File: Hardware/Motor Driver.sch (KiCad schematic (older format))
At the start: 18 parts, among them U4 DRV8874

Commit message: schematic fixed
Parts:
- removed C10: 1uF, Resistor_SMD:R_0603_1608Metric, symbol Device:C_Small
- removed C13: 10uF, Capacitor_SMD:C_2220_5650Metric, symbol Device:C_Small
- removed C17: 100nF, Resistor_SMD:R_0603_1608Metric, symbol Device:C_Small
- removed C20: 22nF, Resistor_SMD:R_0603_1608Metric, symbol Device:C_Small
- removed R13: 5.5k, Resistor_SMD:R_0603_1608Metric, symbol Device:R_Small_US
- removed R14: 16k, Resistor_SMD:R_0603_1608Metric, symbol Device:R_Small_US
- removed R17: 50k, Resistor_SMD:R_0603_1608Metric, symbol Device:R_Small_US
- removed R9: 10k, Resistor_SMD:R_0603_1608Metric, symbol Device:R_Small_US
- removed U4: DRV8874, Package_SO:HTSSOP-16-1EP_4.4x5mm_P0.65mm_EP3.4x5mm_Mask3x3mm_ThermalVias, symbol Driver_Motor:DRV8874
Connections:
- wire segments 50 -> 25
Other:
- moved on the sheet: C10, C13, C17, C20, R13, R14, R17, R9

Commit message: Readme updated
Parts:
- renumbered C10 to C14, C13 to C15, C17 to C16, C20 to C17, R9 to R11, R13 to R12, R14 to R13, R17 to R14, U4 to U5
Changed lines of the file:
@@
 P 5850 4500
 AR Path="/5FF172EF" Ref="#PWR?"  Part="1"
-AR Path="/5FF00151/5FF172EF" Ref="#PWR039"  Part="1"
-AR Path="/5FF2CF13/5FF172EF" Ref="#PWR039"  Part="1"
-F 0 "#PWR039" H 5850 4250 50  0001 C CNN
+AR Path="/5FF00151/5FF172EF" Ref="#PWR027"  Part="1"
+AR Path="/5FF2CF13/5FF172EF" Ref="#PWR036"  Part="1"
+F 0 "#PWR036" H 5850 4250 50  0001 C CNN
 F 1 "GND" H 5855 4327 50  0000 C CNN
 F 2 "" H 5850 4500 50  0001 C CNN
@@
 AR Path="/5EA2026E/5FF2BF81" Ref="C?"  Part="1"
 AR Path="/5FF2BF81" Ref="C?"  Part="1"
-AR Path="/5FF00151/5FF2BF81" Ref="C20"  Part="1"
-AR Path="/5FF2CF13/5FF2BF81" Ref="C20"  Part="1"
-F 0 "C20" H 6542 3396 50  0000 L CNN
+AR Path="/5FF00151/5FF2BF81" Ref="C17"  Part="1"
+AR Path="/5FF2CF13/5FF2BF81" Ref="C21"  Part="1"
+F 0 "C21" H 6542 3396 50  0000 L CNN
 F 1 "22nF" H 6542 3305 50  0000 L CNN
 F 2 "Resistor_SMD:R_0603_1608Metric" H 6450 3350 50  0001 C CNN
@@
 P 4850 4400
 AR Path="/5FF2D4A0" Ref="#PWR?"  Part="1"
-AR Path="/5FF00151/5FF2D4A0" Ref="#PWR038"  Part="1"
-AR Path="/5FF2CF13/5FF2D4A0" Ref="#PWR038"  Part="1"
-F 0 "#PWR038" H 4850 4250 50  0001 C CNN
+AR Path="/5FF00151/5FF2D4A0" Ref="#PWR026"  Part="1"
+AR Path="/5FF2CF13/5FF2D4A0" Ref="#PWR035"  Part="1"
+F 0 "#PWR035" H 4850 4250 50  0001 C CNN
 F 1 "+3.3V" H 4865 4573 50  0000 C CNN
 F 2 "" H 4850 4400 50  0001 C CNN
@@
 P 5000 4450
 AR Path="/5FF172DB" Ref="R?"  Part="1"
-AR Path="/5FF00151/5FF172DB" Ref="R14"  Part="1"
-AR Path="/5FF2CF13/5FF172DB" Ref="R14"  Part="1"
-F 0 "R14" V 5100 4450 50  0000 C CNN
+AR Path="/5FF00151/5FF172DB" Ref="R13"  Part="1"
+AR Path="/5FF2CF13/5FF172DB" Ref="R17"  Part="1"
+F 0 "R17" V 5100 4450 50  0000 C CNN
 F 1 "16k" V 4900 4450 50  0000 C CNN
 F 2 "Resistor_SMD:R_0603_1608Metric" H 5000 4450 50  0001 C CNN
@@
 P 7400 2750
 AR Path="/5FF2D498" Ref="#PWR?"  Part="1"
-AR Path="/5FF00151/5FF2D498" Ref="#PWR018"  Part="1"
-AR Path="/5FF2CF13/5FF2D498" Ref="#PWR018"  Part="1"
-F 0 "#PWR018" H 7200 2600 50  0001 C CNN
+AR Path="/5FF00151/5FF2D498" Ref="#PWR020"  Part="1"
+AR Path="/5FF2CF13/5FF2D498" Ref="#PWR029"  Part="1"
+F 0 "#PWR029" H 7200 2600 50  0001 C CNN
 F 1 "Vdrive" H 7415 2923 50  0000 C CNN
 F 2 "" H 7400 2750 50  0001 C CNN
@@
 P 7100 2750
 AR Path="/5FF172EC" Ref="#PWR?"  Part="1"
-AR Path="/5FF00151/5FF172EC" Ref="#PWR016"  Part="1"
-AR Path="/5FF2CF13/5FF172EC" Ref="#PWR016"  Part="1"
-F 0 "#PWR016" H 6900 2600 50  0001 C CNN
+AR Path="/5FF00151/5FF172EC" Ref="#PWR019"  Part="1"
+AR Path="/5FF2CF13/5FF172EC" Ref="#PWR028"  Part="1"
+F 0 "#PWR028" H 6900 2600 50  0001 C CNN
 F 1 "Vdrive" H 7115 2923 50  0000 C CNN
 F 2 "" H 7100 2750 50  0001 C CNN
@@
 P 7100 2850
 AR Path="/5FF172D6" Ref="C?"  Part="1"
-AR Path="/5FF00151/5FF172D6" Ref="C10"  Part="1"
-AR Path="/5FF2CF13/5FF172D6" Ref="C10"  Part="1"
-F 0 "C10" H 7192 2896 50  0000 L CNN
+AR Path="/5FF00151/5FF172D6" Ref="C14"  Part="1"
+AR Path="/5FF2CF13/5FF172D6" Ref="C18"  Part="1"
+F 0 "C18" H 7192 2896 50  0000 L CNN
 F 1 "1uF" H 7192 2805 50  0000 L CNN
 F 2 "Resistor_SMD:R_0603_1608Metric" H 7100 2850 50  0001 C CNN
@@
 P 7100 2950
 AR Path="/5FF2BF19" Ref="#PWR?"  Part="1"
-AR Path="/5FF00151/5FF2BF19" Ref="#PWR026"  Part="1"
-AR Path="/5FF2CF13/5FF2BF19" Ref="#PWR026"  Part="1"
-F 0 "#PWR026" H 7100 2700 50  0001 C CNN
+AR Path="/5FF00151/5FF2BF19" Ref="#PWR022"  Part="1"
+AR Path="/5FF2CF13/5FF2BF19" Ref="#PWR031"  Part="1"
+F 0 "#PWR031" H 7100 2700 50  0001 C CNN
 F 1 "GND" H 7105 2777 50  0000 C CNN
 F 2 "" H 7100 2950 50  0001 C CNN
@@
 P 7400 2950
 AR Path="/5FF2D48C" Ref="#PWR?"  Part="1"
-AR Path="/5FF00151/5FF2D48C" Ref="#PWR027"  Part="1"
-AR Path="/5FF2CF13/5FF2D48C" Ref="#PWR027"  Part="1"
-F 0 "#PWR027" H 7400 2700 50  0001 C CNN
+AR Path="/5FF00151/5FF2D48C" Ref="#PWR023"  Part="1"
+AR Path="/5FF2CF13/5FF2D48C" Ref="#PWR032"  Part="1"
+F 0 "#PWR032" H 7400 2700 50  0001 C CNN
 F 1 "GND" H 7405 2777 50  0000 C CNN
 F 2 "" H 7400 2950 50  0001 C CNN
@@
 P 5000 4050
 AR Path="/5FF2D49F" Ref="#PWR?"  Part="1"
-AR Path="/5FF00151/5FF2D49F" Ref="#PWR035"  Part="1"
-AR Path="/5FF2CF13/5FF2D49F" Ref="#PWR035"  Part="1"
-F 0 "#PWR035" H 5000 3800 50  0001 C CNN
+AR Path="/5FF00151/5FF2D49F" Ref="#PWR025"  Part="1"
+AR Path="/5FF2CF13/5FF2D49F" Ref="#PWR034"  Part="1"
+F 0 "#PWR034" H 5000 3800 50  0001 C CNN
 F 1 "GND" V 5005 3922 50  0000 R CNN
 F 2 "" H 5000 4050 50  0001 C CNN
@@
 AR Path="/5EA2026E/5FF2D494" Ref="R?"  Part="1"
 AR Path="/5FF2D494" Ref="R?"  Part="1"
-AR Path="/5FF00151/5FF2D494" Ref="R9"  Part="1"
-AR Path="/5FF2CF13/5FF2D494" Ref="R9"  Part="1"
-F 0 "R9" H 4968 3646 50  0000 L CNN
+AR Path="/5FF00151/5FF2D494" Ref="R11"  Part="1"
+AR Path="/5FF2CF13/5FF2D494" Ref="R15"  Part="1"
+F 0 "R15" H 4968 3646 50  0000 L CNN
 F 1 "10k" H 4968 3555 50  0000 L CNN
 F 2 "Resistor_SMD:R_0603_1608Metric" H 4900 3600 50  0001 C CNN
@@
 P 7400 2850
 AR Path="/5FF2D490" Ref="C?"  Part="1"
-AR Path="/5FF00151/5FF2D490" Ref="C13"  Part="1"
-AR Path="/5FF2CF13/5FF2D490" Ref="C13"  Part="1"
-F 0 "C13" H 7492 2896 50  0000 L CNN
+AR Path="/5FF00151/5FF2D490" Ref="C15"  Part="1"
+AR Path="/5FF2CF13/5FF2D490" Ref="C19"  Part="1"
+F 0 "C19" H 7492 2896 50  0000 L CNN
 F 1 "10uF" H 7492 2805 50  0000 L CNN
 F 2 "Capacitor_SMD:C_2220_5650Metric" H 7400 2850 50  0001 C CNN
@@
 P 5850 3050
 AR Path="/5FF172F1" Ref="U?"  Part="1"
-AR Path="/5FF00151/5FF172F1" Ref="U4"  Part="1"
-AR Path="/5FF2CF13/5FF172F1" Ref="U4"  Part="1"
-F 0 "U4" H 6250 3250 50  0000 C CNN
+AR Path="/5FF00151/5FF172F1" Ref="U5"  Part="1"
+AR Path="/5FF2CF13/5FF172F1" Ref="U6"  Part="1"
+F 0 "U6" H 6250 3250 50  0000 C CNN
 F 1 "DRV8874" H 6250 3150 50  0000 C CNN
 F 2 "Package_SO:HTSSOP-16-1EP_4.4x5mm_P0.65mm_EP3.4x5mm_Mask3x3mm_ThermalVias" H 6200 3200 50  0001 C CNN
@@
 P 4900 3500
 AR Path="/5FF172E1" Ref="#PWR?"  Part="1"
-AR Path="/5FF00151/5FF172E1" Ref="#PWR030"  Part="1"
-AR Path="/5FF2CF13/5FF172E1" Ref="#PWR030"  Part="1"
-F 0 "#PWR030" H 4900 3350 50  0001 C CNN
+AR Path="/5FF00151/5FF172E1" Ref="#PWR024"  Part="1"
+AR Path="/5FF2CF13/5FF172E1" Ref="#PWR033"  Part="1"
+F 0 "#PWR033" H 4900 3350 50  0001 C CNN
 F 1 "+3.3V" H 4915 3673 50  0000 C CNN
 F 2 "" H 4900 3500 50  0001 C CNN
@@
 P 5100 4050
 AR Path="/5FF2D49E" Ref="R?"  Part="1"
-AR Path="/5FF00151/5FF2D49E" Ref="R13"  Part="1"
-AR Path="/5FF2CF13/5FF2D49E" Ref="R13"  Part="1"
-F 0 "R13" V 5050 3950 50  0000 C CNN
+AR Path="/5FF00151/5FF2D49E" Ref="R12"  Part="1"
+AR Path="/5FF2CF13/5FF2D49E" Ref="R16"  Part="1"
+F 0 "R16" V 5050 3950 50  0000 C CNN
 F 1 "5.5k" V 5050 4150 50  0000 C CNN
 F 2 "Resistor_SMD:R_0603_1608Metric" H 5100 4050 50  0001 C CNN
@@
 P 5300 4450
 AR Path="/5FF172DD" Ref="R?"  Part="1"
-AR Path="/5FF00151/5FF172DD" Ref="R17"  Part="1"
-AR Path="/5FF2CF13/5FF172DD" Ref="R17"  Part="1"
-F 0 "R17" V 5400 4450 50  0000 C CNN
+AR Path="/5FF00151/5FF172DD" Ref="R14"  Part="1"
+AR Path="/5FF2CF13/5FF172DD" Ref="R18"  Part="1"
+F 0 "R18" V 5400 4450 50  0000 C CNN
 F 1 "50k" V 5200 4450 50  0000 C CNN
 F 2 "Resistor_SMD:R_0603_1608Metric" H 5300 4450 50  0001 C CNN
@@
 P 6000 2850
 AR Path="/5FF2D4A1" Ref="#PWR?"  Part="1"
-AR Path="/5FF00151/5FF2D4A1" Ref="#PWR023"  Part="1"
-AR Path="/5FF2CF13/5FF2D4A1" Ref="#PWR023"  Part="1"
-F 0 "#PWR023" H 5800 2700 50  0001 C CNN
+AR Path="/5FF00151/5FF2D4A1" Ref="#PWR021"  Part="1"
+AR Path="/5FF2CF13/5FF2D4A1" Ref="#PWR030"  Part="1"
+F 0 "#PWR030" H 5800 2700 50  0001 C CNN
 F 1 "Vdrive" H 6015 3023 50  0000 C CNN
 F 2 "" H 6000 2850 50  0001 C CNN
@@
 P 5850 2900
 AR Path="/5FF2D4A2" Ref="C?"  Part="1"
-AR Path="/5FF00151/5FF2D4A2" Ref="C17"  Part="1"
-AR Path="/5FF2CF13/5FF2D4A2" Ref="C17"  Part="1"
-F 0 "C17" V 5650 2800 50  0000 C CNN
+AR Path="/5FF00151/5FF2D4A2" Ref="C16"  Part="1"
+AR Path="/5FF2CF13/5FF2D4A2" Ref="C20"  Part="1"
+F 0 "C20" V 5650 2800 50  0000 C CNN
 F 1 "100nF" V 5750 2800 50  0000 C CNN
 F 2 "Resistor_SMD:R_0603_1608Metric" H 5850 2900 50  0001 C CNN

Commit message: Signed-off-by: Usman Mehmood <usmanmehmood55@gmail.com>
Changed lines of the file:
@@
 $Descr A4 11693 8268
 encoding utf-8
-Sheet 6 6
+Sheet 2 9
 Title ""
 Date ""
@@
 AR Path="/5FF00151/5FF172EF" Ref="#PWR027"  Part="1"
 AR Path="/5FF2CF13/5FF172EF" Ref="#PWR036"  Part="1"
-F 0 "#PWR036" H 5850 4250 50  0001 C CNN
+F 0 "#PWR027" H 5850 4250 50  0001 C CNN
 F 1 "GND" H 5855 4327 50  0000 C CNN
 F 2 "" H 5850 4500 50  0001 C CNN
@@
 AR Path="/5FF00151/5FF2BF81" Ref="C17"  Part="1"
 AR Path="/5FF2CF13/5FF2BF81" Ref="C21"  Part="1"
-F 0 "C21" H 6542 3396 50  0000 L CNN
+F 0 "C17" H 6542 3396 50  0000 L CNN
 F 1 "22nF" H 6542 3305 50  0000 L CNN
 F 2 "Resistor_SMD:R_0603_1608Metric" H 6450 3350 50  0001 C CNN
@@
 AR Path="/5FF00151/5FF2D4A0" Ref="#PWR026"  Part="1"
 AR Path="/5FF2CF13/5FF2D4A0" Ref="#PWR035"  Part="1"
-F 0 "#PWR035" H 4850 4250 50  0001 C CNN
+F 0 "#PWR026" H 4850 4250 50  0001 C CNN
 F 1 "+3.3V" H 4865 4573 50  0000 C CNN
 F 2 "" H 4850 4400 50  0001 C CNN
@@
 AR Path="/5FF00151/5FF172DB" Ref="R13"  Part="1"
 AR Path="/5FF2CF13/5FF172DB" Ref="R17"  Part="1"
-F 0 "R17" V 5100 4450 50  0000 C CNN
+F 0 "R13" V 5100 4450 50  0000 C CNN
 F 1 "16k" V 4900 4450 50  0000 C CNN
 F 2 "Resistor_SMD:R_0603_1608Metric" H 5000 4450 50  0001 C CNN
@@
 AR Path="/5FF00151/5FF2D498" Ref="#PWR020"  Part="1"
 AR Path="/5FF2CF13/5FF2D498" Ref="#PWR029"  Part="1"
-F 0 "#PWR029" H 7200 2600 50  0001 C CNN
+F 0 "#PWR020" H 7200 2600 50  0001 C CNN
 F 1 "Vdrive" H 7415 2923 50  0000 C CNN
 F 2 "" H 7400 2750 50  0001 C CNN
@@
 AR Path="/5FF00151/5FF172EC" Ref="#PWR019"  Part="1"
 AR Path="/5FF2CF13/5FF172EC" Ref="#PWR028"  Part="1"
-F 0 "#PWR028" H 6900 2600 50  0001 C CNN
+F 0 "#PWR019" H 6900 2600 50  0001 C CNN
 F 1 "Vdrive" H 7115 2923 50  0000 C CNN
 F 2 "" H 7100 2750 50  0001 C CNN
@@
 AR Path="/5FF00151/5FF172D6" Ref="C14"  Part="1"
 AR Path="/5FF2CF13/5FF172D6" Ref="C18"  Part="1"
-F 0 "C18" H 7192 2896 50  0000 L CNN
+F 0 "C14" H 7192 2896 50  0000 L CNN
 F 1 "1uF" H 7192 2805 50  0000 L CNN
 F 2 "Resistor_SMD:R_0603_1608Metric" H 7100 2850 50  0001 C CNN
@@
 AR Path="/5FF00151/5FF2BF19" Ref="#PWR022"  Part="1"
 AR Path="/5FF2CF13/5FF2BF19" Ref="#PWR031"  Part="1"
-F 0 "#PWR031" H 7100 2700 50  0001 C CNN
+F 0 "#PWR022" H 7100 2700 50  0001 C CNN
 F 1 "GND" H 7105 2777 50  0000 C CNN
 F 2 "" H 7100 2950 50  0001 C CNN
@@
 AR Path="/5FF00151/5FF2D48C" Ref="#PWR023"  Part="1"
 AR Path="/5FF2CF13/5FF2D48C" Ref="#PWR032"  Part="1"
-F 0 "#PWR032" H 7400 2700 50  0001 C CNN
+F 0 "#PWR023" H 7400 2700 50  0001 C CNN
 F 1 "GND" H 7405 2777 50  0000 C CNN
 F 2 "" H 7400 2950 50  0001 C CNN
@@
 AR Path="/5FF00151/5FF2D49F" Ref="#PWR025"  Part="1"
 AR Path="/5FF2CF13/5FF2D49F" Ref="#PWR034"  Part="1"
-F 0 "#PWR034" H 5000 3800 50  0001 C CNN
+F 0 "#PWR025" H 5000 3800 50  0001 C CNN
 F 1 "GND" V 5005 3922 50  0000 R CNN
 F 2 "" H 5000 4050 50  0001 C CNN
@@
 AR Path="/5FF00151/5FF2D494" Ref="R11"  Part="1"
 AR Path="/5FF2CF13/5FF2D494" Ref="R15"  Part="1"
-F 0 "R15" H 4968 3646 50  0000 L CNN
+F 0 "R11" H 4968 3646 50  0000 L CNN
 F 1 "10k" H 4968 3555 50  0000 L CNN
 F 2 "Resistor_SMD:R_0603_1608Metric" H 4900 3600 50  0001 C CNN
@@
 AR Path="/5FF00151/5FF2D490" Ref="C15"  Part="1"
 AR Path="/5FF2CF13/5FF2D490" Ref="C19"  Part="1"
-F 0 "C19" H 7492 2896 50  0000 L CNN
+F 0 "C15" H 7492 2896 50  0000 L CNN
 F 1 "10uF" H 7492 2805 50  0000 L CNN
 F 2 "Capacitor_SMD:C_2220_5650Metric" H 7400 2850 50  0001 C CNN
@@
 	1    0    0    -1
 $EndComp
-$Comp
-L Driver_Motor:DRV8874 U?
-U 1 1 5FF172F1
-P 5850 3050
-AR Path="/5FF172F1" Ref="U?"  Part="1"
-AR Path="/5FF00151/5FF172F1" Ref="U5"  Part="1"
-AR Path="/5FF2CF13/5FF172F1" Ref="U6"  Part="1"
-F 0 "U6" H 6250 3250 50  0000 C CNN
-F 1 "DRV8874" H 6250 3150 50  0000 C CNN
-F 2 "Package_SO:HTSSOP-16-1EP_4.4x5mm_P0.65mm_EP3.4x5mm_Mask3x3mm_ThermalVias" H 6200 3200 50  0001 C CNN
-F 3 "" H 6200 3200 50  0001 C CNN
-	1    5850 3050
-	1    0    0    -1
-$EndComp
 Text HLabel 5200 3900 0    50   Output ~ 0
 iPROPI
@@
 AR Path="/5FF00151/5FF172E1" Ref="#PWR024"  Part="1"
 AR Path="/5FF2CF13/5FF172E1" Ref="#PWR033"  Part="1"
-F 0 "#PWR033" H 4900 3350 50  0001 C CNN
+F 0 "#PWR024" H 4900 3350 50  0001 C CNN
 F 1 "+3.3V" H 4915 3673 50  0000 C CNN
 F 2 "" H 4900 3500 50  0001 C CNN
@@
 AR Path="/5FF00151/5FF2D49E" Ref="R12"  Part="1"
 AR Path="/5FF2CF13/5FF2D49E" Ref="R16"  Part="1"
-F 0 "R16" V 5050 3950 50  0000 C CNN
+F 0 "R12" V 5050 3950 50  0000 C CNN
 F 1 "5.5k" V 5050 4150 50  0000 C CNN
 F 2 "Resistor_SMD:R_0603_1608Metric" H 5100 4050 50  0001 C CNN
@@
 AR Path="/5FF00151/5FF172DD" Ref="R14"  Part="1"
 AR Path="/5FF2CF13/5FF172DD" Ref="R18"  Part="1"
-F 0 "R18" V 5400 4450 50  0000 C CNN
+F 0 "R14" V 5400 4450 50  0000 C CNN
 F 1 "50k" V 5200 4450 50  0000 C CNN
 F 2 "Resistor_SMD:R_0603_1608Metric" H 5300 4450 50  0001 C CNN
@@
 AR Path="/5FF00151/5FF2D4A1" Ref="#PWR021"  Part="1"
 AR Path="/5FF2CF13/5FF2D4A1" Ref="#PWR030"  Part="1"
-F 0 "#PWR030" H 5800 2700 50  0001 C CNN
+F 0 "#PWR021" H 5800 2700 50  0001 C CNN
 F 1 "Vdrive" H 6015 3023 50  0000 C CNN
 F 2 "" H 6000 2850 50  0001 C CNN
@@
 AR Path="/5FF00151/5FF2D4A2" Ref="C16"  Part="1"
 AR Path="/5FF2CF13/5FF2D4A2" Ref="C20"  Part="1"
-F 0 "C20" V 5650 2800 50  0000 C CNN
+F 0 "C16" V 5650 2800 50  0000 C CNN
 F 1 "100nF" V 5750 2800 50  0000 C CNN
 F 2 "Resistor_SMD:R_0603_1608Metric" H 5850 2900 50  0001 C CNN
@@
 	0    1    1    0
 $EndComp
+$Comp
+L Driver_Motor:DRV8874 U?
+U 1 1 5FF172F1
+P 5850 3050
+AR Path="/5FF172F1" Ref="U?"  Part="1"
+AR Path="/5FF00151/5FF172F1" Ref="U5"  Part="1"
+AR Path="/5FF2CF13/5FF172F1" Ref="U6"  Part="1"
+F 0 "U5" H 6250 3250 50  0000 C CNN
+F 1 "DRV8874" H 6250 3150 50  0000 C CNN
+F 2 "Package_SO:HTSSOP-16-1EP_4.4x5mm_P0.65mm_EP3.4x5mm_Mask3x3mm_ThermalVias" H 6200 3200 50  0001 C CNN
+F 3 "" H 6200 3200 50  0001 C CNN
+	1    5850 3050
+	1    0    0    -1
+$EndComp
 $EndSCHEMATC

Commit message: Tidying up
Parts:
- U5: symbol Driver_Motor:DRV8874 -> drv8874:DRV8874
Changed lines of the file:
@@
 $EndComp
 $Comp
-L Driver_Motor:DRV8874 U?
+L drv8874:DRV8874 U?
 U 1 1 5FF172F1
 P 5850 3050

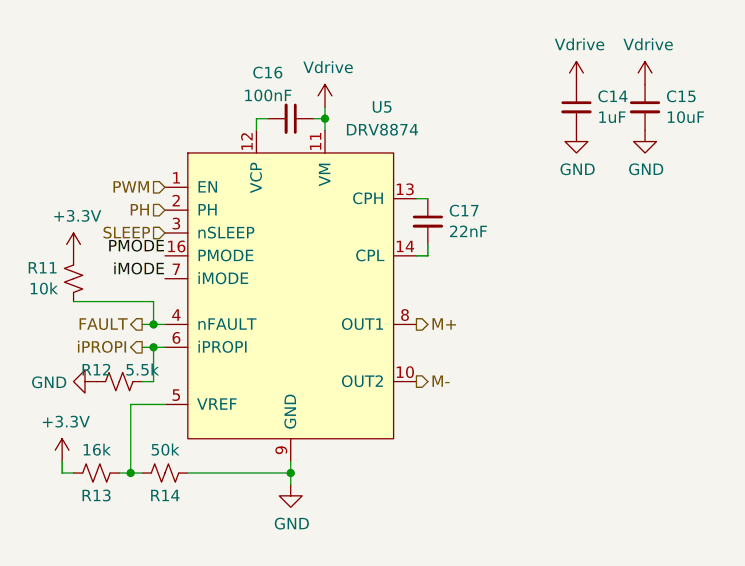
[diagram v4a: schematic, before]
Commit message: Battery charger IC added
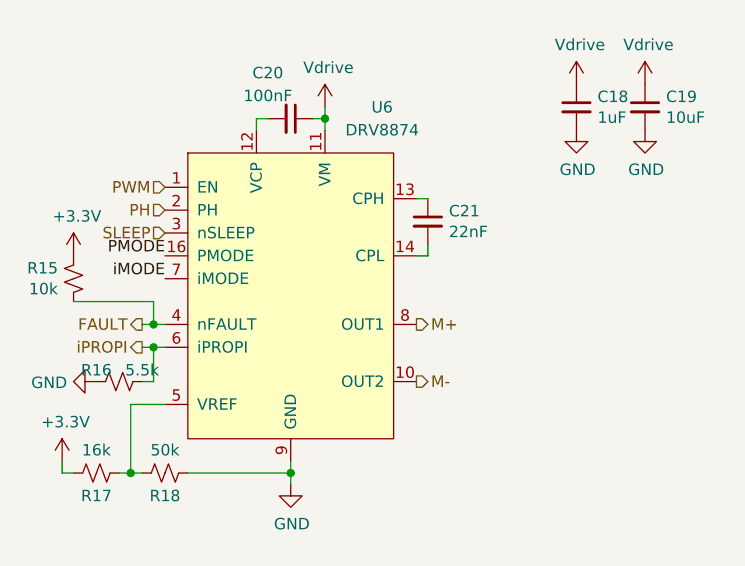
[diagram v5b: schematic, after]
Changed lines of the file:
@@
 AR Path="/5FF00151/5FF172EF" Ref="#PWR027"  Part="1"
 AR Path="/5FF2CF13/5FF172EF" Ref="#PWR036"  Part="1"
-F 0 "#PWR027" H 5850 4250 50  0001 C CNN
+F 0 "#PWR036" H 5850 4250 50  0001 C CNN
 F 1 "GND" H 5855 4327 50  0000 C CNN
 F 2 "" H 5850 4500 50  0001 C CNN
@@
 AR Path="/5FF00151/5FF2BF81" Ref="C17"  Part="1"
 AR Path="/5FF2CF13/5FF2BF81" Ref="C21"  Part="1"
-F 0 "C17" H 6542 3396 50  0000 L CNN
+F 0 "C21" H 6542 3396 50  0000 L CNN
 F 1 "22nF" H 6542 3305 50  0000 L CNN
 F 2 "Resistor_SMD:R_0603_1608Metric" H 6450 3350 50  0001 C CNN
@@
 AR Path="/5FF00151/5FF2D4A0" Ref="#PWR026"  Part="1"
 AR Path="/5FF2CF13/5FF2D4A0" Ref="#PWR035"  Part="1"
-F 0 "#PWR026" H 4850 4250 50  0001 C CNN
+F 0 "#PWR035" H 4850 4250 50  0001 C CNN
 F 1 "+3.3V" H 4865 4573 50  0000 C CNN
 F 2 "" H 4850 4400 50  0001 C CNN
@@
 AR Path="/5FF00151/5FF172DB" Ref="R13"  Part="1"
 AR Path="/5FF2CF13/5FF172DB" Ref="R17"  Part="1"
-F 0 "R13" V 5100 4450 50  0000 C CNN
+F 0 "R17" V 5100 4450 50  0000 C CNN
 F 1 "16k" V 4900 4450 50  0000 C CNN
 F 2 "Resistor_SMD:R_0603_1608Metric" H 5000 4450 50  0001 C CNN
@@
 AR Path="/5FF00151/5FF2D498" Ref="#PWR020"  Part="1"
 AR Path="/5FF2CF13/5FF2D498" Ref="#PWR029"  Part="1"
-F 0 "#PWR020" H 7200 2600 50  0001 C CNN
+F 0 "#PWR029" H 7200 2600 50  0001 C CNN
 F 1 "Vdrive" H 7415 2923 50  0000 C CNN
 F 2 "" H 7400 2750 50  0001 C CNN
@@
 AR Path="/5FF00151/5FF172EC" Ref="#PWR019"  Part="1"
 AR Path="/5FF2CF13/5FF172EC" Ref="#PWR028"  Part="1"
-F 0 "#PWR019" H 6900 2600 50  0001 C CNN
+F 0 "#PWR028" H 6900 2600 50  0001 C CNN
 F 1 "Vdrive" H 7115 2923 50  0000 C CNN
 F 2 "" H 7100 2750 50  0001 C CNN
@@
 AR Path="/5FF00151/5FF172D6" Ref="C14"  Part="1"
 AR Path="/5FF2CF13/5FF172D6" Ref="C18"  Part="1"
-F 0 "C14" H 7192 2896 50  0000 L CNN
+F 0 "C18" H 7192 2896 50  0000 L CNN
 F 1 "1uF" H 7192 2805 50  0000 L CNN
 F 2 "Resistor_SMD:R_0603_1608Metric" H 7100 2850 50  0001 C CNN
@@
 AR Path="/5FF00151/5FF2BF19" Ref="#PWR022"  Part="1"
 AR Path="/5FF2CF13/5FF2BF19" Ref="#PWR031"  Part="1"
-F 0 "#PWR022" H 7100 2700 50  0001 C CNN
+F 0 "#PWR031" H 7100 2700 50  0001 C CNN
 F 1 "GND" H 7105 2777 50  0000 C CNN
 F 2 "" H 7100 2950 50  0001 C CNN
@@
 AR Path="/5FF00151/5FF2D48C" Ref="#PWR023"  Part="1"
 AR Path="/5FF2CF13/5FF2D48C" Ref="#PWR032"  Part="1"
-F 0 "#PWR023" H 7400 2700 50  0001 C CNN
+F 0 "#PWR032" H 7400 2700 50  0001 C CNN
 F 1 "GND" H 7405 2777 50  0000 C CNN
 F 2 "" H 7400 2950 50  0001 C CNN
@@
 AR Path="/5FF00151/5FF2D49F" Ref="#PWR025"  Part="1"
 AR Path="/5FF2CF13/5FF2D49F" Ref="#PWR034"  Part="1"
-F 0 "#PWR025" H 5000 3800 50  0001 C CNN
+F 0 "#PWR034" H 5000 3800 50  0001 C CNN
 F 1 "GND" V 5005 3922 50  0000 R CNN
 F 2 "" H 5000 4050 50  0001 C CNN
@@
 AR Path="/5FF00151/5FF2D494" Ref="R11"  Part="1"
 AR Path="/5FF2CF13/5FF2D494" Ref="R15"  Part="1"
-F 0 "R11" H 4968 3646 50  0000 L CNN
+F 0 "R15" H 4968 3646 50  0000 L CNN
 F 1 "10k" H 4968 3555 50  0000 L CNN
 F 2 "Resistor_SMD:R_0603_1608Metric" H 4900 3600 50  0001 C CNN
@@
 AR Path="/5FF00151/5FF2D490" Ref="C15"  Part="1"
 AR Path="/5FF2CF13/5FF2D490" Ref="C19"  Part="1"
-F 0 "C15" H 7492 2896 50  0000 L CNN
+F 0 "C19" H 7492 2896 50  0000 L CNN
 F 1 "10uF" H 7492 2805 50  0000 L CNN
 F 2 "Capacitor_SMD:C_2220_5650Metric" H 7400 2850 50  0001 C CNN
@@
 AR Path="/5FF00151/5FF172E1" Ref="#PWR024"  Part="1"
 AR Path="/5FF2CF13/5FF172E1" Ref="#PWR033"  Part="1"
-F 0 "#PWR024" H 4900 3350 50  0001 C CNN
+F 0 "#PWR033" H 4900 3350 50  0001 C CNN
 F 1 "+3.3V" H 4915 3673 50  0000 C CNN
 F 2 "" H 4900 3500 50  0001 C CNN
@@
 AR Path="/5FF00151/5FF2D49E" Ref="R12"  Part="1"
 AR Path="/5FF2CF13/5FF2D49E" Ref="R16"  Part="1"
-F 0 "R12" V 5050 3950 50  0000 C CNN
+F 0 "R16" V 5050 3950 50  0000 C CNN
 F 1 "5.5k" V 5050 4150 50  0000 C CNN
 F 2 "Resistor_SMD:R_0603_1608Metric" H 5100 4050 50  0001 C CNN
@@
 AR Path="/5FF00151/5FF172DD" Ref="R14"  Part="1"
 AR Path="/5FF2CF13/5FF172DD" Ref="R18"  Part="1"
-F 0 "R14" V 5400 4450 50  0000 C CNN
+F 0 "R18" V 5400 4450 50  0000 C CNN
 F 1 "50k" V 5200 4450 50  0000 C CNN
 F 2 "Resistor_SMD:R_0603_1608Metric" H 5300 4450 50  0001 C CNN
@@
 AR Path="/5FF00151/5FF2D4A1" Ref="#PWR021"  Part="1"
 AR Path="/5FF2CF13/5FF2D4A1" Ref="#PWR030"  Part="1"
-F 0 "#PWR021" H 5800 2700 50  0001 C CNN
+F 0 "#PWR030" H 5800 2700 50  0001 C CNN
 F 1 "Vdrive" H 6015 3023 50  0000 C CNN
 F 2 "" H 6000 2850 50  0001 C CNN
@@
 AR Path="/5FF00151/5FF2D4A2" Ref="C16"  Part="1"
 AR Path="/5FF2CF13/5FF2D4A2" Ref="C20"  Part="1"
-F 0 "C16" V 5650 2800 50  0000 C CNN
+F 0 "C20" V 5650 2800 50  0000 C CNN
 F 1 "100nF" V 5750 2800 50  0000 C CNN
 F 2 "Resistor_SMD:R_0603_1608Metric" H 5850 2900 50  0001 C CNN
@@
 AR Path="/5FF00151/5FF172F1" Ref="U5"  Part="1"
 AR Path="/5FF2CF13/5FF172F1" Ref="U6"  Part="1"
-F 0 "U5" H 6250 3250 50  0000 C CNN
+F 0 "U6" H 6250 3250 50  0000 C CNN
 F 1 "DRV8874" H 6250 3150 50  0000 C CNN
 F 2 "Package_SO:HTSSOP-16-1EP_4.4x5mm_P0.65mm_EP3.4x5mm_Mask3x3mm_ThermalVias" H 6200 3200 50  0001 C CNN
